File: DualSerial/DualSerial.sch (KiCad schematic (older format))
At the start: 22 parts, among them CN1 DB9 Male, CN2 DB9 Male, J1 COM_A_SELECT, J2 IRQ_A_SELECT, J3 COM_A_SELECT, J4 IRQ_B_SELECT, J5 Bus_ISA_8bit, U1 16550/16C550, U2 GAL16V8, U3 GD75232N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

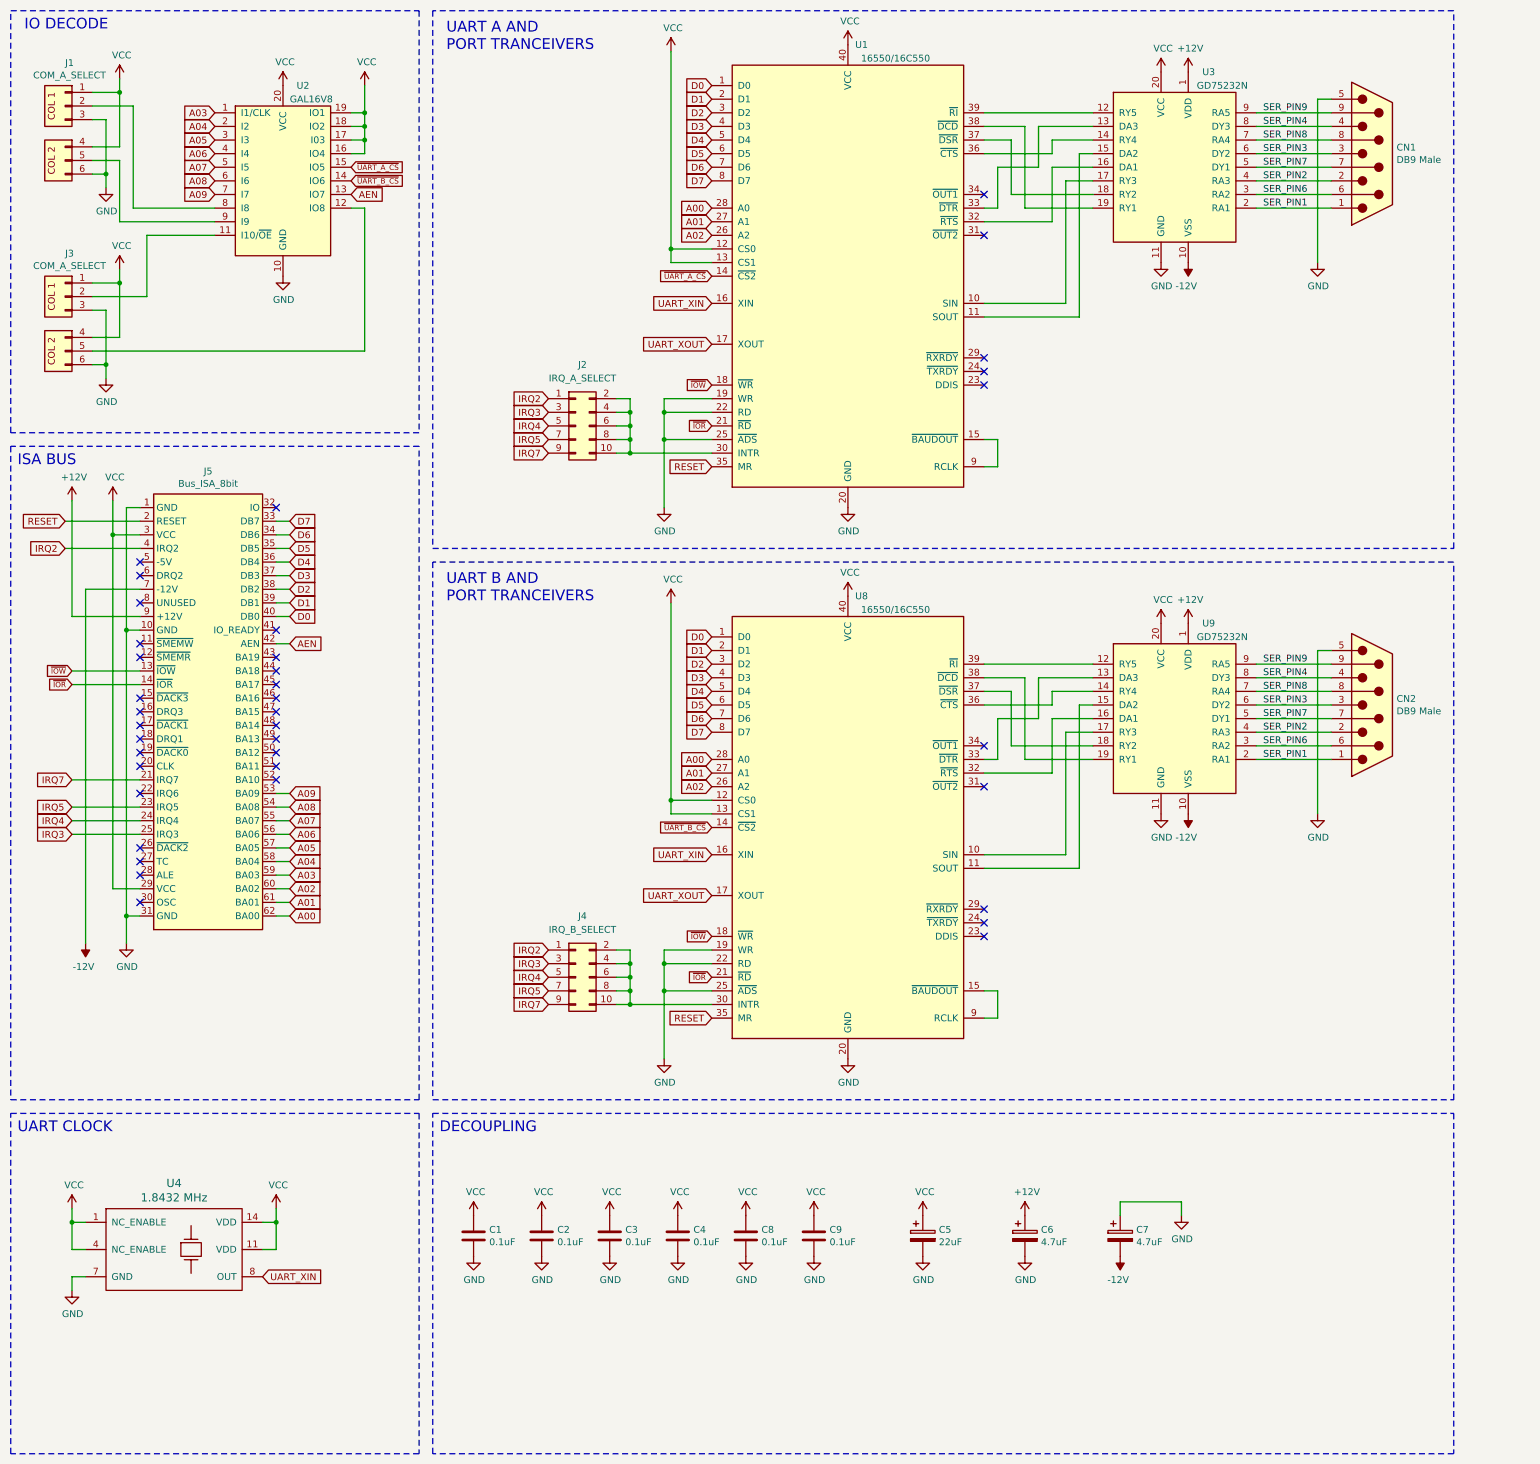
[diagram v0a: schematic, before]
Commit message: DualSerial: Add debug output signal for whether A and B port are configured the same.
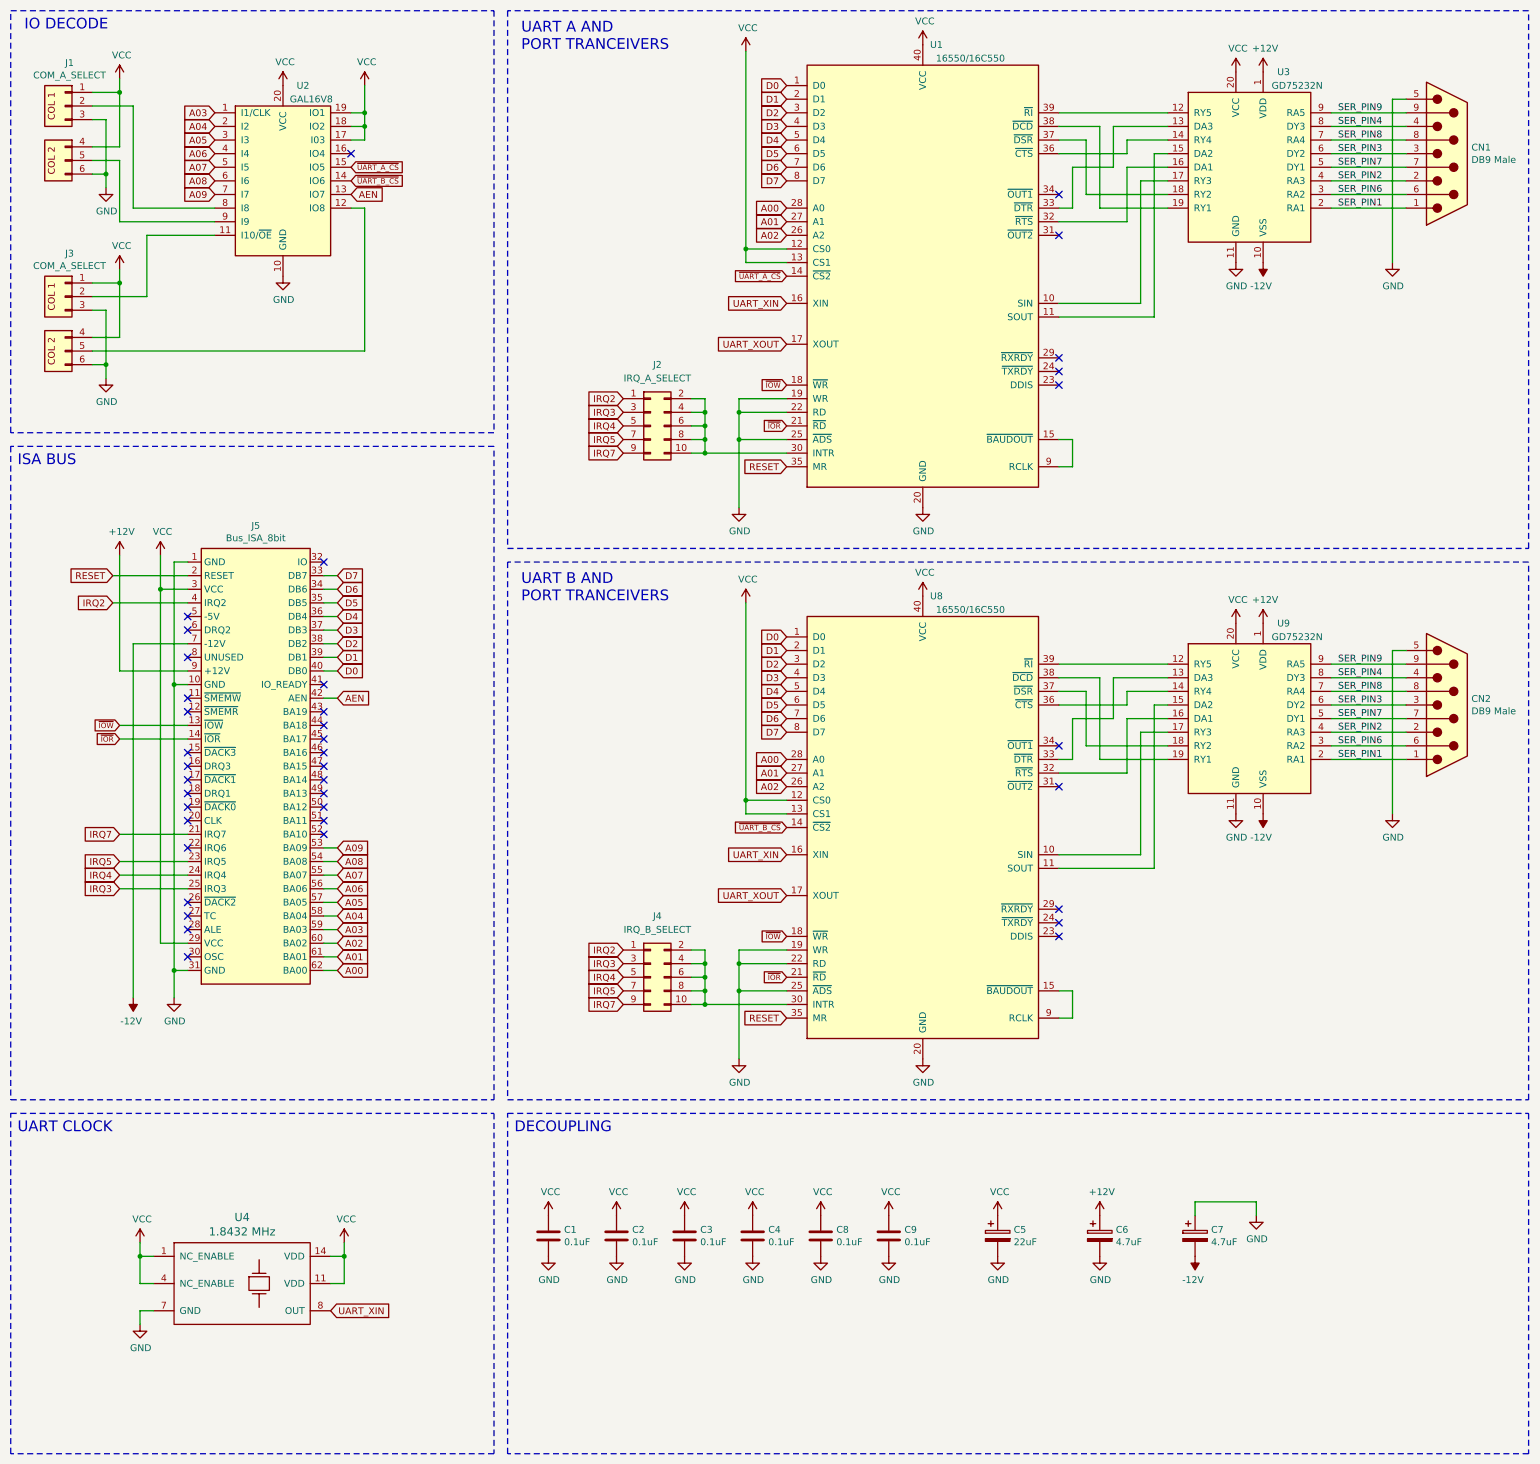
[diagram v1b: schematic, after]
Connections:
- net VCC: no longer U2.16 (IO4)
- no-connect marks 38 -> 39
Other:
- moved on the sheet: C1, C2, C3, C4, C5, C6, C7, C8, C9, CN1, CN2, J2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

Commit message: DualSerial: WIP on PCB layout.
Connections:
- net ~UART_A_CS: now also U2.14 (IO6); no longer U2.15 (IO5)
- net ~UART_B_CS: now also U2.15 (IO5); no longer U2.14 (IO6)
- net at U2.11 (I10/~OE~): now also J3.5 (Pin_5); no longer J3.2 (Pin_2)
- net at U2.12 (IO8): now also J3.2 (Pin_2); no longer J3.5 (Pin_5)
- net UART_A_B_SAME_PORT: now reaches U2.16 (IO4)
- net SER_PIN1 renamed SERA_PIN1
- net SERA_PIN1: no longer CN2.1, U9.2 (RA1)
- net SER_PIN2 renamed SERA_PIN2
- net SERA_PIN2: no longer CN2.2, U9.4 (RA3)
- net SER_PIN3 renamed SERA_PIN3
- net SERA_PIN3: no longer CN2.3, U9.6 (DY2)
- net SER_PIN4 renamed SERA_PIN4
- net SERA_PIN4: no longer CN2.4, U9.8 (DY3)
- net SER_PIN6 renamed SERA_PIN6
- net SERA_PIN6: no longer CN2.6, U9.3 (RA2)
- net SER_PIN7 renamed SERA_PIN7
- net SERA_PIN7: no longer CN2.7, U9.5 (DY1)
- net SER_PIN8 renamed SERA_PIN8
- net SERA_PIN8: no longer CN2.8, U9.7 (RA4)
- net SER_PIN9 renamed SERA_PIN9
- net SERA_PIN9: no longer CN2.9, U9.9 (RA5)
- net UART_XOUT: no longer names the net of U1.17 (XOUT)
- net UART_XOUT: no longer U8.17 (XOUT)
- new net SERB_PIN1: CN2.1, U9.2 (RA1)
- new net SERB_PIN2: CN2.2, U9.4 (RA3)
- new net SERB_PIN3: CN2.3, U9.6 (DY2)
- new net SERB_PIN4: CN2.4, U9.8 (DY3)
- new net SERB_PIN6: CN2.6, U9.3 (RA2)
- new net SERB_PIN7: CN2.7, U9.5 (DY1)
- new net SERB_PIN8: CN2.8, U9.7 (RA4)
- new net SERB_PIN9: CN2.9, U9.9 (RA5)
- no-connect marks 39 -> 42
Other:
- moved on the sheet: C1, C2, C3, C4, C5, C6, C7, C8, C9

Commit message: DualSerial: More WIP on PCB layout.
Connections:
- net SERA_PIN1: now also U3.9 (RA5); no longer U3.2 (RA1)
- net SERA_PIN4: now also U3.5 (DY1); no longer U3.8 (DY3)
- net SERA_PIN6: now also U3.7 (RA4); no longer U3.3 (RA2)
- net SERA_PIN7: now also U3.8 (DY3); no longer U3.5 (DY1)
- net SERA_PIN8: now also U3.3 (RA2); no longer U3.7 (RA4)
- net SERA_PIN9: now also U3.2 (RA1); no longer U3.9 (RA5)
- net SERB_PIN1: now also U9.9 (RA5); no longer U9.2 (RA1)
- net SERB_PIN4: now also U9.5 (DY1); no longer U9.8 (DY3)
- net SERB_PIN6: now also U9.7 (RA4); no longer U9.3 (RA2)
- net SERB_PIN7: now also U9.8 (DY3); no longer U9.5 (DY1)
- net SERB_PIN8: now also U9.3 (RA2); no longer U9.7 (RA4)
- net SERB_PIN9: now also U9.2 (RA1); no longer U9.9 (RA5)
- net at U1.32 (~RTS~): now also U3.13 (DA3); no longer U3.16 (DA1)
- net at U1.33 (~DTR~): now also U3.16 (DA1); no longer U3.13 (DA3)
- net at U1.36 (~CTS~): now also U3.18 (RY2); no longer U3.14 (RY4)
- net at U1.37 (~DSR~): now also U3.14 (RY4); no longer U3.18 (RY2)
- net at U1.38 (~DCD~): now also U3.12 (RY5); no longer U3.19 (RY1)
- net at U1.39 (~RI~): now also U3.19 (RY1); no longer U3.12 (RY5)
- net at U8.32 (~RTS~): now also U9.13 (DA3); no longer U9.16 (DA1)
- net at U8.33 (~DTR~): now also U9.16 (DA1); no longer U9.13 (DA3)
- net at U8.36 (~CTS~): now also U9.18 (RY2); no longer U9.14 (RY4)
- net at U8.37 (~DSR~): now also U9.14 (RY4); no longer U9.18 (RY2)
- net at U8.38 (~DCD~): now also U9.12 (RY5); no longer U9.19 (RY1)
- net at U8.39 (~RI~): now also U9.19 (RY1); no longer U9.12 (RY5)
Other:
- note added: "UART A\nAND PORT\nTRANCEIVERS"
- note added: "UART B\nAND PORT\nTRANCEIVERS"
- note removed: "UART A AND\nPORT TRANCEIVERS"
- note removed: "UART B AND\nPORT TRANCEIVERS"
- moved on the sheet: CN2, J2, J4, U1, U8, U9

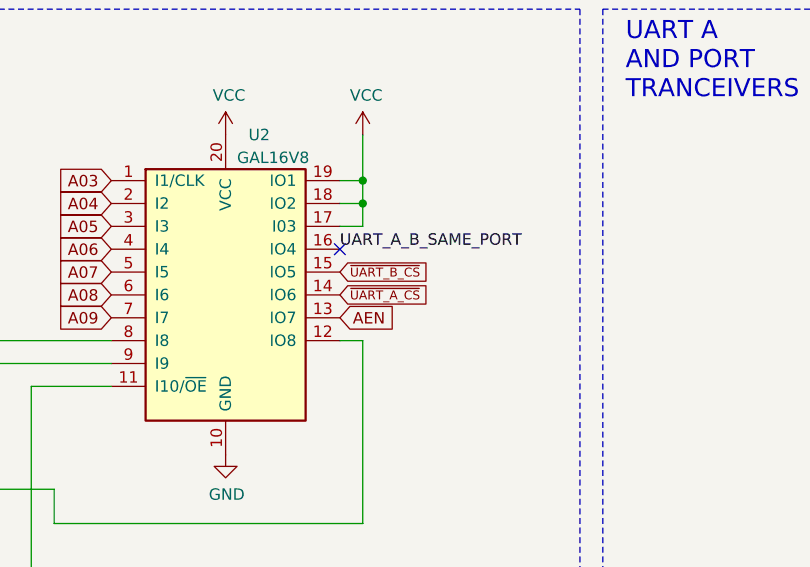
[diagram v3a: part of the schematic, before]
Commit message: Dual Serial: Flip A and B ports to correct location.
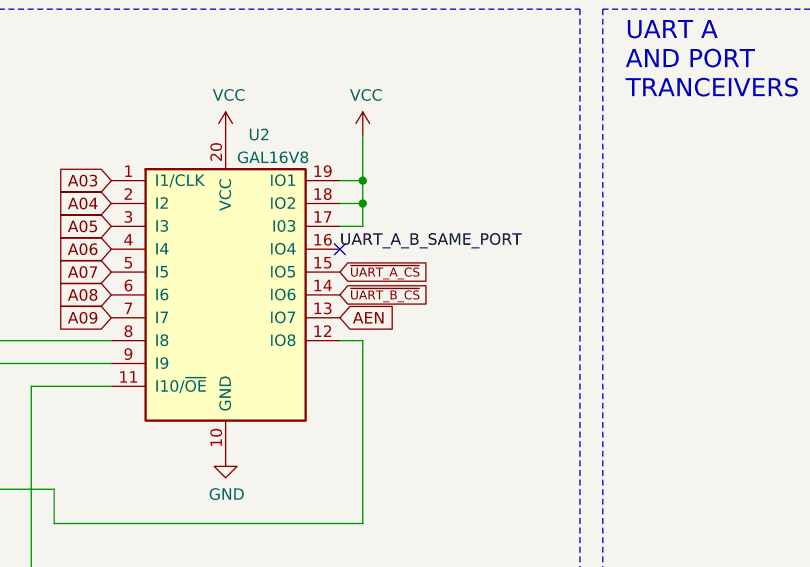
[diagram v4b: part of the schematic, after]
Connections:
- net ~UART_A_CS: now also U2.15 (IO5); no longer U2.14 (IO6)
- net ~UART_B_CS: now also U2.14 (IO6); no longer U2.15 (IO5)
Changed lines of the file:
@@
 Text GLabel 3050 1900 2    50   Input ~ 0
 AEN
+Text GLabel 3050 1700 2    39   Input ~ 0
+~UART_A_CS
 Text GLabel 3050 1800 2    39   Input ~ 0
-~UART_A_CS
-Text GLabel 3050 1700 2    39   Input ~ 0
 ~UART_B_CS
 Wire Wire Line
@@
 	10950 1400 10850 1400
 $Comp
-L power:GND #PWR?
+L power:GND #PWR0107
 U 1 1 61101C60
 P 10850 2600
-F 0 "#PWR?" H 10850 2350 50  0001 C CNN
+F 0 "#PWR0107" H 10850 2350 50  0001 C CNN
 F 1 "GND" H 10855 2427 50  0000 C CNN
 F 2 "" H 10850 2600 50  0001 C CNN
@@
 $EndComp
 $Comp
-L power:-12V #PWR?
+L power:-12V #PWR0108
 U 1 1 61101C74
 P 9100 2400
-F 0 "#PWR?" H 9100 2500 50  0001 C CNN
+F 0 "#PWR0108" H 9100 2500 50  0001 C CNN
 F 1 "-12V" H 9115 2573 50  0000 C CNN
 F 2 "" H 9100 2400 50  0001 C CNN
@@
 $EndComp
 $Comp
-L power:GND #PWR?
+L power:GND #PWR0109
 U 1 1 61101C7E
 P 8900 2400
-F 0 "#PWR?" H 8900 2150 50  0001 C CNN
+F 0 "#PWR0109" H 8900 2150 50  0001 C CNN
 F 1 "GND" H 8905 2227 50  0000 C CNN
 F 2 "" H 8900 2400 50  0001 C CNN
@@
 $EndComp
 $Comp
-L power:VCC #PWR?
+L power:VCC #PWR0111
 U 1 1 61101C88
 P 8900 1000
-F 0 "#PWR?" H 8900 850 50  0001 C CNN
+F 0 "#PWR0111" H 8900 850 50  0001 C CNN
 F 1 "VCC" H 8915 1173 50  0000 C CNN
 F 2 "" H 8900 1000 50  0001 C CNN
@@
 $EndComp
 $Comp
-L power:+12V #PWR?
+L power:+12V #PWR0120
 U 1 1 61101C92
 P 9100 1000
-F 0 "#PWR?" H 9100 850 50  0001 C CNN
+F 0 "#PWR0120" H 9100 850 50  0001 C CNN
 F 1 "+12V" H 9115 1173 50  0000 C CNN
 F 2 "" H 9100 1000 50  0001 C CNN
